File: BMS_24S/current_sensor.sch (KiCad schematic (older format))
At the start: 11 parts, among them J3102 Current_Conn, J3103 BSPD_Conn, U3101 LM324

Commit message: get BSPD
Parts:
- removed C3101: 100nF, Capacitor_SMD:C_0805_2012Metric, symbol Device:C
- added unit 4 of U3101
- R3105: LCSC C17414 -> C17477
- U3101: LCSC (none) -> C71035
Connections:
- net -5V is gone; now on net GND: U3101.11 (V-)
- net GND: now also U3101.12 (+), U3101.13 (-)
- no-connect marks 3 -> 4
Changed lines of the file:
@@
 F 2 "Package_SO:SOIC-14_3.9x8.7mm_P1.27mm" H 4800 1625 50  0001 C CNN
 F 3 "http://www.ti.com/lit/ds/symlink/lm2902-n.pdf" H 4850 2100 50  0001 C CNN
+F 4 "C71035" H 4800 1900 50  0001 C CNN "LCSC"
 	1    4800 1900
 	1    0    0    -1
@@
 	1    5250 3250
 	1    0    0    -1
-$EndComp
-$Comp
-L power:-5V #PWR03104
-U 1 1 5F371489
-P 4450 3450
-F 0 "#PWR03104" H 4450 3550 50  0001 C CNN
-F 1 "-5V" H 4465 3623 50  0000 C CNN
-F 2 "" H 4450 3450 50  0001 C CNN
-F 3 "" H 4450 3450 50  0001 C CNN
-	1    4450 3450
-	-1   0    0    1
 $EndComp
 Text HLabel 4700 1600 2    50   Input ~ 0
@@
 F 2 "Package_SO:SOIC-14_3.9x8.7mm_P1.27mm" H 4850 3175 50  0001 C CNN
 F 3 "http://www.ti.com/lit/ds/symlink/lm2902-n.pdf" H 4900 3650 50  0001 C CNN
+F 4 "C71035" H 4850 3450 50  0001 C CNN "LCSC"
 	5    4850 3450
 	0    1    1    0
@@
 	5150 3350 5250 3350
 $Comp
-L Device:C C?
-U 1 1 5F37C448
-P 4200 3600
-AR Path="/5EA47040/5F37C448" Ref="C?"  Part="1"
-AR Path="/5EA471BF/5F37C448" Ref="C?"  Part="1"
-AR Path="/5EEF4361/5F37C448" Ref="C?"  Part="1"
-AR Path="/5EEF524D/5F37C448" Ref="C?"  Part="1"
-AR Path="/5EC044AE/5EC054C7/5F37C448" Ref="C?"  Part="1"
-AR Path="/5EC044AE/5EC39151/5F37C448" Ref="C?"  Part="1"
-AR Path="/5EC24961/5EC054C7/5F37C448" Ref="C?"  Part="1"
-AR Path="/5EC24961/5EC3A225/5F37C448" Ref="C?"  Part="1"
-AR Path="/5EC24961/5EC4031A/5F37C448" Ref="C?"  Part="1"
-AR Path="/5EC24961/5EC462FD/5F37C448" Ref="C?"  Part="1"
-AR Path="/5EC24961/5EC4BDFE/5F37C448" Ref="C?"  Part="1"
-AR Path="/5EC24961/5EC51A1F/5F37C448" Ref="C?"  Part="1"
-AR Path="/5EC24961/5EC574F6/5F37C448" Ref="C?"  Part="1"
-AR Path="/5EC24961/5EC5D2D3/5F37C448" Ref="C?"  Part="1"
-AR Path="/5EC24961/5EC62E5E/5F37C448" Ref="C?"  Part="1"
-AR Path="/5EC24961/5EC6897D/5F37C448" Ref="C?"  Part="1"
-AR Path="/5EC24961/5EC6E4EA/5F37C448" Ref="C?"  Part="1"
-AR Path="/5EC24961/5EC74033/5F37C448" Ref="C?"  Part="1"
-AR Path="/5EC24961/5EC79B70/5F37C448" Ref="C?"  Part="1"
-AR Path="/5EC24961/5EC7F6A7/5F37C448" Ref="C?"  Part="1"
-AR Path="/5EC24961/5EC85226/5F37C448" Ref="C?"  Part="1"
-AR Path="/5F3561B0/5F37C448" Ref="C3101"  Part="1"
-F 0 "C3101" H 4315 3646 50  0000 L CNN
-F 1 "100nF" H 4315 3555 50  0000 L CNN
-F 2 "Capacitor_SMD:C_0805_2012Metric" H 4238 3450 50  0001 C CNN
-F 3 "https://datasheet.lcsc.com/szlcsc/YAGEO-CC0805KRX7R9BB104_C49678.pdf" H 4200 3600 50  0001 C CNN
-F 4 "C49678" H 4200 3600 50  0001 C CNN "LCSC"
-F 5 "10%" H 4200 3600 50  0001 C CNN "Precision"
-F 6 "50V" H 4200 3600 50  0001 C CNN "Voltage"
-	1    4200 3600
-	-1   0    0    -1
-$EndComp
-$Comp
 L power:GND #PWR03105
 U 1 1 5F37C9E9
-P 4200 3850
-F 0 "#PWR03105" H 4200 3600 50  0001 C CNN
-F 1 "GND" H 4205 3677 50  0000 C CNN
-F 2 "" H 4200 3850 50  0001 C CNN
-F 3 "" H 4200 3850 50  0001 C CNN
-	1    4200 3850
+P 4200 3550
+F 0 "#PWR03105" H 4200 3300 50  0001 C CNN
+F 1 "GND" H 4205 3377 50  0000 C CNN
+F 2 "" H 4200 3550 50  0001 C CNN
+F 3 "" H 4200 3550 50  0001 C CNN
+	1    4200 3550
 	1    0    0    -1
 $EndComp
@@
 $EndComp
 Wire Wire Line
-	4200 3850 4200 3750
-Wire Wire Line
-	4450 3450 4450 3350
-Wire Wire Line
-	4450 3350 4550 3350
-Wire Wire Line
 	5250 3250 5250 3350
 Wire Wire Line
@@
 Text HLabel 5550 3350 2    50   Input ~ 0
 +5V
-Text HLabel 4100 3350 0    50   Input ~ 0
--5V
-Wire Wire Line
-	4100 3350 4200 3350
-Wire Wire Line
-	4200 3350 4200 3450
-Connection ~ 4200 3350
 Wire Wire Line
 	5450 3450 5450 3350
@@
 	5450 3350 5550 3350
 Connection ~ 5450 3350
-Wire Wire Line
-	4200 3350 4450 3350
-Connection ~ 4450 3350
 Wire Wire Line
 	5250 3350 5450 3350
@@
 F 2 "Package_SO:SOIC-14_3.9x8.7mm_P1.27mm" H 4800 2175 50  0001 C CNN
 F 3 "http://www.ti.com/lit/ds/symlink/lm2902-n.pdf" H 4850 2650 50  0001 C CNN
+F 4 "C71035" H 4800 2450 50  0001 C CNN "LCSC"
 	2    4800 2450
 	1    0    0    -1
@@
 F 2 "Package_SO:SOIC-14_3.9x8.7mm_P1.27mm" H 6700 1725 50  0001 C CNN
 F 3 "http://www.ti.com/lit/ds/symlink/lm2902-n.pdf" H 6750 2200 50  0001 C CNN
+F 4 "C71035" H 6700 2000 50  0001 C CNN "LCSC"
 	3    6700 2000
 	1    0    0    1
@@
 F 3 "~" H 4450 1600 50  0001 C CNN
 F 4 "1%" V 4250 1600 50  0001 C CNN "Precision"
-F 5 "C17414" H 4450 1600 50  0001 C CNN "LCSC"
+F 5 "C17477" H 4450 1600 50  0001 C CNN "LCSC"
 F 6 "1/8W" H 4450 1600 50  0001 C CNN "Power"
 F 7 "150V" H 4450 1600 50  0001 C CNN "Voltage"
@@
 	0    1    1    0
 $EndComp
+$Comp
+L e-Power:LM324 U?
+U 4 1 5F58B9DC
+P 6700 3200
+AR Path="/5EA47040/5F58B9DC" Ref="U?"  Part="1"
+AR Path="/5EA471BF/5F58B9DC" Ref="U?"  Part="1"
+AR Path="/5EEF4361/5F58B9DC" Ref="U?"  Part="1"
+AR Path="/5EEF524D/5F58B9DC" Ref="U?"  Part="1"
+AR Path="/5EC044AE/5EC054C7/5F58B9DC" Ref="U?"  Part="1"
+AR Path="/5EC044AE/5EC39151/5F58B9DC" Ref="U?"  Part="1"
+AR Path="/5EC24961/5EC054C7/5F58B9DC" Ref="U?"  Part="1"
+AR Path="/5EC24961/5EC3A225/5F58B9DC" Ref="U?"  Part="1"
+AR Path="/5EC24961/5EC4031A/5F58B9DC" Ref="U?"  Part="1"
+AR Path="/5EC24961/5EC462FD/5F58B9DC" Ref="U?"  Part="1"
+AR Path="/5EC24961/5EC4BDFE/5F58B9DC" Ref="U?"  Part="1"
+AR Path="/5EC24961/5EC51A1F/5F58B9DC" Ref="U?"  Part="1"
+AR Path="/5EC24961/5EC574F6/5F58B9DC" Ref="U?"  Part="1"
+AR Path="/5EC24961/5EC5D2D3/5F58B9DC" Ref="U?"  Part="1"
+AR Path="/5EC24961/5EC62E5E/5F58B9DC" Ref="U?"  Part="1"
+AR Path="/5EC24961/5EC6897D/5F58B9DC" Ref="U?"  Part="1"
+AR Path="/5EC24961/5EC6E4EA/5F58B9DC" Ref="U?"  Part="1"
+AR Path="/5EC24961/5EC74033/5F58B9DC" Ref="U?"  Part="1"
+AR Path="/5EC24961/5EC79B70/5F58B9DC" Ref="U?"  Part="1"
+AR Path="/5EC24961/5EC7F6A7/5F58B9DC" Ref="U?"  Part="1"
+AR Path="/5EC24961/5EC85226/5F58B9DC" Ref="U?"  Part="1"
+AR Path="/5F3561B0/5F58B9DC" Ref="U3101"  Part="4"
+F 0 "U3101" H 6800 3050 50  0000 C CNN
+F 1 "LM324" H 6700 3200 50  0000 C CNN
+F 2 "Package_SO:SOIC-14_3.9x8.7mm_P1.27mm" H 6700 2925 50  0001 C CNN
+F 3 "http://www.ti.com/lit/ds/symlink/lm2902-n.pdf" H 6750 3400 50  0001 C CNN
+F 4 "C71035" H 6700 3200 50  0001 C CNN "LCSC"
+	4    6700 3200
+	1    0    0    1
+$EndComp
+$Comp
+L power:GND #PWR0176
+U 1 1 5F58CCF6
+P 6300 3400
+F 0 "#PWR0176" H 6300 3150 50  0001 C CNN
+F 1 "GND" H 6305 3227 50  0000 C CNN
+F 2 "" H 6300 3400 50  0001 C CNN
+F 3 "" H 6300 3400 50  0001 C CNN
+	1    6300 3400
+	1    0    0    -1
+$EndComp
+Wire Wire Line
+	6300 3400 6300 3300
+Wire Wire Line
+	6300 3100 6400 3100
+Wire Wire Line
+	6400 3300 6300 3300
+Connection ~ 6300 3300
+Wire Wire Line
+	6300 3300 6300 3100
+NoConn ~ 7000 3200
+Wire Wire Line
+	4200 3350 4550 3350
+Wire Wire Line
+	4200 3350 4200 3550
 $EndSCHEMATC

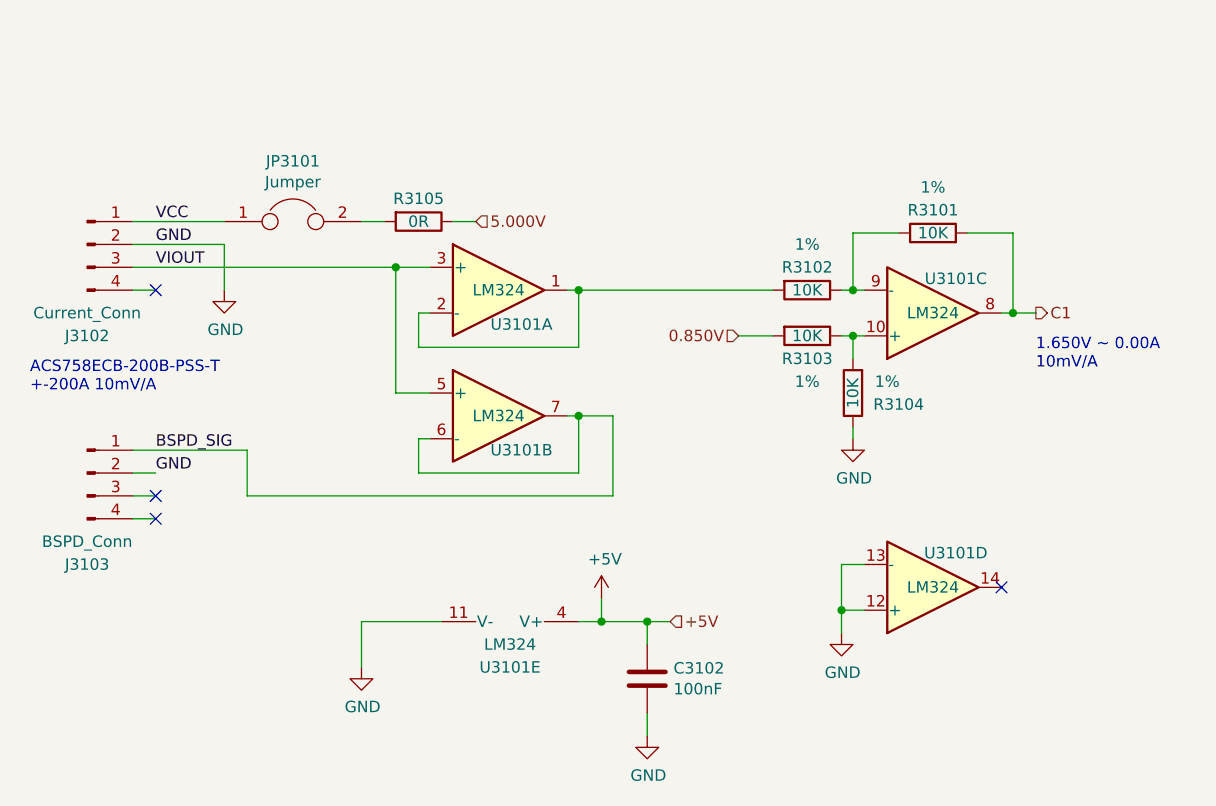
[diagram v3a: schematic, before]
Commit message: update bms pcb
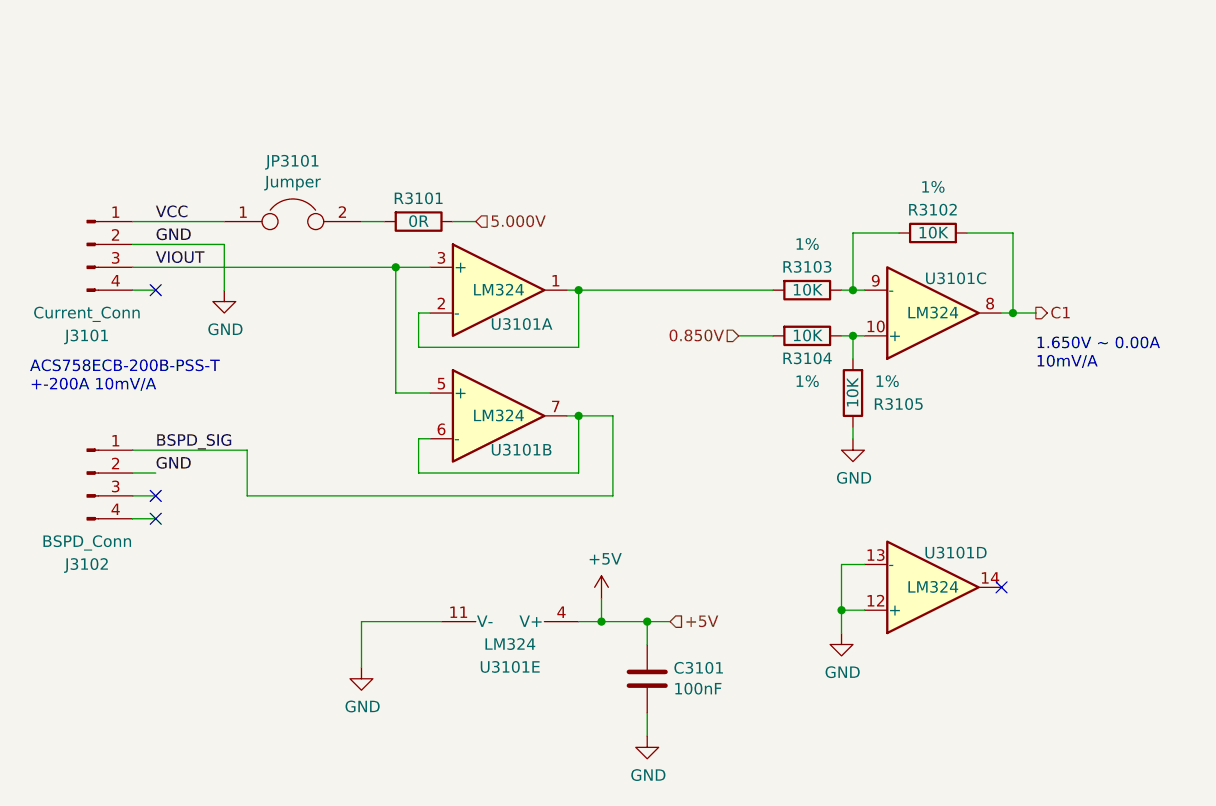
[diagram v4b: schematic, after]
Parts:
- renumbered C3102 to C3101, J3102 to J3101, J3103 to J3102, R3105 to R3101, R3101 to R3102, R3102 to R3103, R3103 to R3104, R3104 to R3105
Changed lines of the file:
@@
 $EndDescr
 $Comp
-L Connector:Conn_01x04_Male J3102
+L Connector:Conn_01x04_Male J3101
 U 1 1 5F3568F3
 P 3000 1700
-F 0 "J3102" H 3000 1300 50  0000 C CNN
+F 0 "J3101" H 3000 1300 50  0000 C CNN
 F 1 "Current_Conn" H 3000 1400 50  0000 C CNN
 F 2 "Connector_PinHeader_2.54mm:PinHeader_1x04_P2.54mm_Horizontal" H 3000 1700 50  0001 C CNN
@@
 AR Path="/5EC24961/5EC7F6A7/5F37D4F6" Ref="C?"  Part="1"
 AR Path="/5EC24961/5EC85226/5F37D4F6" Ref="C?"  Part="1"
-AR Path="/5F3561B0/5F37D4F6" Ref="C3102"  Part="1"
-F 0 "C3102" H 5565 3646 50  0000 L CNN
+AR Path="/5F3561B0/5F37D4F6" Ref="C3101"  Part="1"
+F 0 "C3101" H 5565 3646 50  0000 L CNN
 F 1 "100nF" H 5565 3555 50  0000 L CNN
 F 2 "Capacitor_SMD:C_0805_2012Metric" H 5488 3450 50  0001 C CNN
@@
 Connection ~ 5150 2450
 $Comp
-L Connector:Conn_01x04_Male J3103
+L Connector:Conn_01x04_Male J3102
 U 1 1 5F189870
 P 3000 2700
-F 0 "J3103" H 3000 2300 50  0000 C CNN
+F 0 "J3102" H 3000 2300 50  0000 C CNN
 F 1 "BSPD_Conn" H 3000 2400 50  0000 C CNN
 F 2 "Connector_PinHeader_2.54mm:PinHeader_1x04_P2.54mm_Horizontal" H 3000 2700 50  0001 C CNN
@@
 AR Path="/5EC24961/5EC7F6A7/5F19D869" Ref="R?"  Part="1"
 AR Path="/5EC24961/5EC85226/5F19D869" Ref="R?"  Part="1"
-AR Path="/5F3561B0/5F19D869" Ref="R3102"  Part="1"
-F 0 "R3102" V 6050 1900 50  0000 C CNN
+AR Path="/5F3561B0/5F19D869" Ref="R3103"  Part="1"
+F 0 "R3103" V 6050 1900 50  0000 C CNN
 F 1 "10K" V 6150 1900 50  0000 C CNN
 F 2 "Resistor_SMD:R_0805_2012Metric" V 6080 1900 50  0001 C CNN
@@
 AR Path="/5EC24961/5EC7F6A7/5F19E141" Ref="R?"  Part="1"
 AR Path="/5EC24961/5EC85226/5F19E141" Ref="R?"  Part="1"
-AR Path="/5F3561B0/5F19E141" Ref="R3103"  Part="1"
-F 0 "R3103" V 6250 2100 50  0000 C CNN
+AR Path="/5F3561B0/5F19E141" Ref="R3104"  Part="1"
+F 0 "R3104" V 6250 2100 50  0000 C CNN
 F 1 "10K" V 6150 2100 50  0000 C CNN
 F 2 "Resistor_SMD:R_0805_2012Metric" V 6080 2100 50  0001 C CNN
@@
 AR Path="/5EC24961/5EC7F6A7/5F19E3C2" Ref="R?"  Part="1"
 AR Path="/5EC24961/5EC85226/5F19E3C2" Ref="R?"  Part="1"
-AR Path="/5F3561B0/5F19E3C2" Ref="R3104"  Part="1"
-F 0 "R3104" H 6150 2400 50  0000 C CNN
+AR Path="/5F3561B0/5F19E3C2" Ref="R3105"  Part="1"
+F 0 "R3105" H 6150 2400 50  0000 C CNN
 F 1 "10K" V 6350 2350 50  0000 C CNN
 F 2 "Resistor_SMD:R_0805_2012Metric" V 6280 2350 50  0001 C CNN
@@
 AR Path="/5EC24961/5EC7F6A7/5F19EB05" Ref="R?"  Part="1"
 AR Path="/5EC24961/5EC85226/5F19EB05" Ref="R?"  Part="1"
-AR Path="/5F3561B0/5F19EB05" Ref="R3101"  Part="1"
-F 0 "R3101" V 6800 1650 50  0000 C CNN
+AR Path="/5F3561B0/5F19EB05" Ref="R3102"  Part="1"
+F 0 "R3102" V 6800 1650 50  0000 C CNN
 F 1 "10K" V 6700 1650 50  0000 C CNN
 F 2 "Resistor_SMD:R_0805_2012Metric" V 6630 1650 50  0001 C CNN
@@
 AR Path="/5EC24961/5EC7F6A7/629BD18A" Ref="R?"  Part="1"
 AR Path="/5EC24961/5EC85226/629BD18A" Ref="R?"  Part="1"
-AR Path="/5F3561B0/629BD18A" Ref="R3105"  Part="1"
-F 0 "R3105" V 4350 1600 50  0000 C CNN
+AR Path="/5F3561B0/629BD18A" Ref="R3101"  Part="1"
+F 0 "R3101" V 4350 1600 50  0000 C CNN
 F 1 "0R" V 4450 1600 50  0000 C CNN
 F 2 "Resistor_SMD:R_0805_2012Metric" V 4380 1600 50  0001 C CNN
@@
 $EndComp
 $Comp
-L power:GND #PWR0176
+L power:GND #PWR03104
 U 1 1 5F58CCF6
 P 6300 3400
-F 0 "#PWR0176" H 6300 3150 50  0001 C CNN
+F 0 "#PWR03104" H 6300 3150 50  0001 C CNN
 F 1 "GND" H 6305 3227 50  0000 C CNN
 F 2 "" H 6300 3400 50  0001 C CNN

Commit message: updates made on BMS
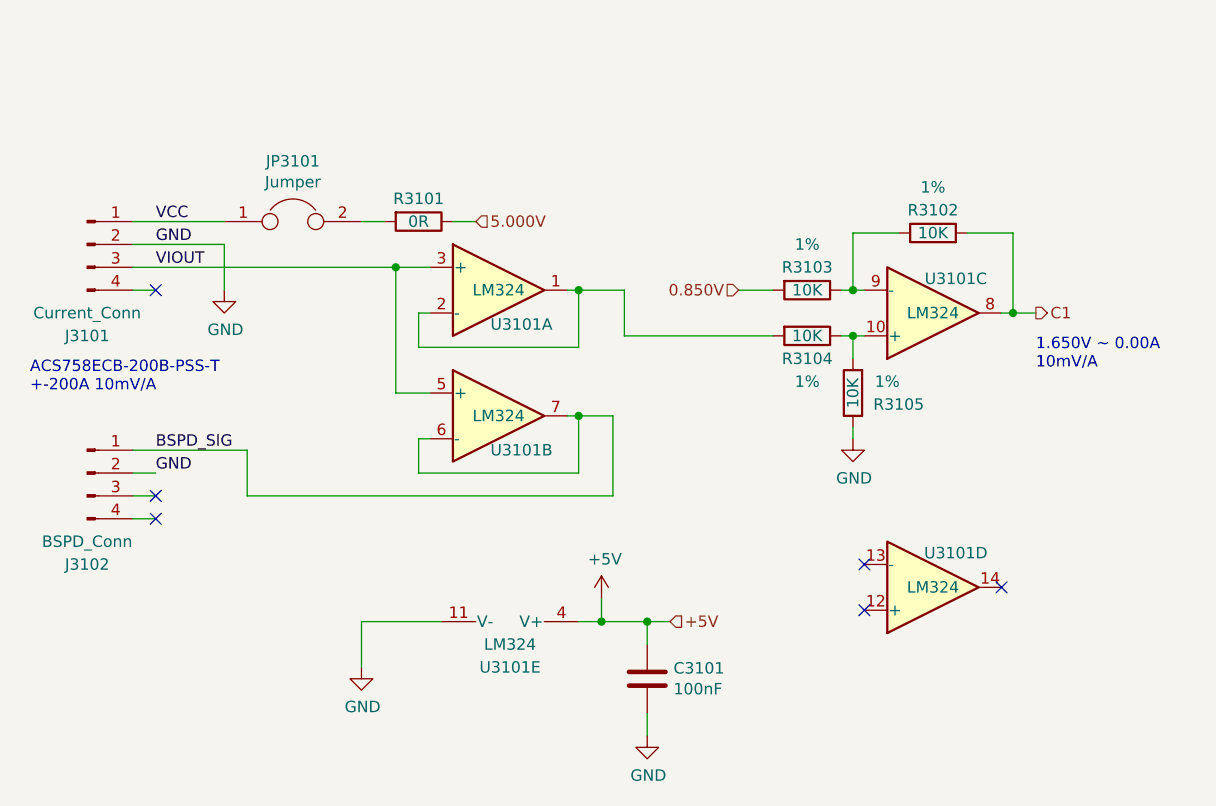
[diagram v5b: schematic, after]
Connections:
- net 0.850V: now also R3103.2; no longer R3104.2
- net GND: no longer U3101.12 (+), U3101.13 (-)
- net at U3101.1, U3101.2 (-): now also R3104.2; no longer R3103.2
- no-connect marks 4 -> 6
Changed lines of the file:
@@
 Wire Wire Line
 	5150 1900 5100 1900
-Connection ~ 5150 1900
 $Comp
 L power:+5V #PWR03103
@@
 	5150 3350 5250 3350
 $Comp
-L power:GND #PWR03105
+L power:GND #PWR03104
 U 1 1 5F37C9E9
 P 4200 3550
-F 0 "#PWR03105" H 4200 3300 50  0001 C CNN
+F 0 "#PWR03104" H 4200 3300 50  0001 C CNN
 F 1 "GND" H 4205 3377 50  0000 C CNN
 F 2 "" H 4200 3550 50  0001 C CNN
@@
 $EndComp
 $Comp
-L power:GND #PWR03106
+L power:GND #PWR03105
 U 1 1 5F37CD3B
 P 5450 3850
-F 0 "#PWR03106" H 5450 3600 50  0001 C CNN
+F 0 "#PWR03105" H 5450 3600 50  0001 C CNN
 F 1 "GND" H 5455 3677 50  0000 C CNN
 F 2 "" H 5450 3850 50  0001 C CNN
@@
 	7050 1650 6850 1650
 Wire Wire Line
-	5150 1900 6000 1900
-Wire Wire Line
 	7050 2000 7150 2000
 Connection ~ 7050 2000
@@
 Text Notes 7150 2250 0    50   ~ 0
 1.650V ~~ 0.00A\n10mV/A\n
-Text HLabel 5850 2100 0    50   Input ~ 0
-0.850V
-Wire Wire Line
-	5850 2100 6000 2100
 $Comp
 L Device:Jumper JP3101
@@
 	1    0    0    1
 $EndComp
-$Comp
-L power:GND #PWR03104
-U 1 1 5F58CCF6
-P 6300 3400
-F 0 "#PWR03104" H 6300 3150 50  0001 C CNN
-F 1 "GND" H 6305 3227 50  0000 C CNN
-F 2 "" H 6300 3400 50  0001 C CNN
-F 3 "" H 6300 3400 50  0001 C CNN
-	1    6300 3400
-	1    0    0    -1
-$EndComp
-Wire Wire Line
-	6300 3400 6300 3300
-Wire Wire Line
-	6300 3100 6400 3100
-Wire Wire Line
-	6400 3300 6300 3300
-Connection ~ 6300 3300
-Wire Wire Line
-	6300 3300 6300 3100
 NoConn ~ 7000 3200
 Wire Wire Line
@@
 Wire Wire Line
 	4200 3350 4200 3550
+NoConn ~ 6400 3100
+NoConn ~ 6400 3300
+Text HLabel 5850 1900 0    50   Input ~ 0
+0.850V
+Wire Wire Line
+	6000 2100 5350 2100
+Wire Wire Line
+	5350 2100 5350 1900
+Wire Wire Line
+	5350 1900 5150 1900
+Connection ~ 5150 1900
+Wire Wire Line
+	5850 1900 6000 1900
 $EndSCHEMATC
